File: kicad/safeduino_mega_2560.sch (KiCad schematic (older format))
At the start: 103 parts, among them X1 USB

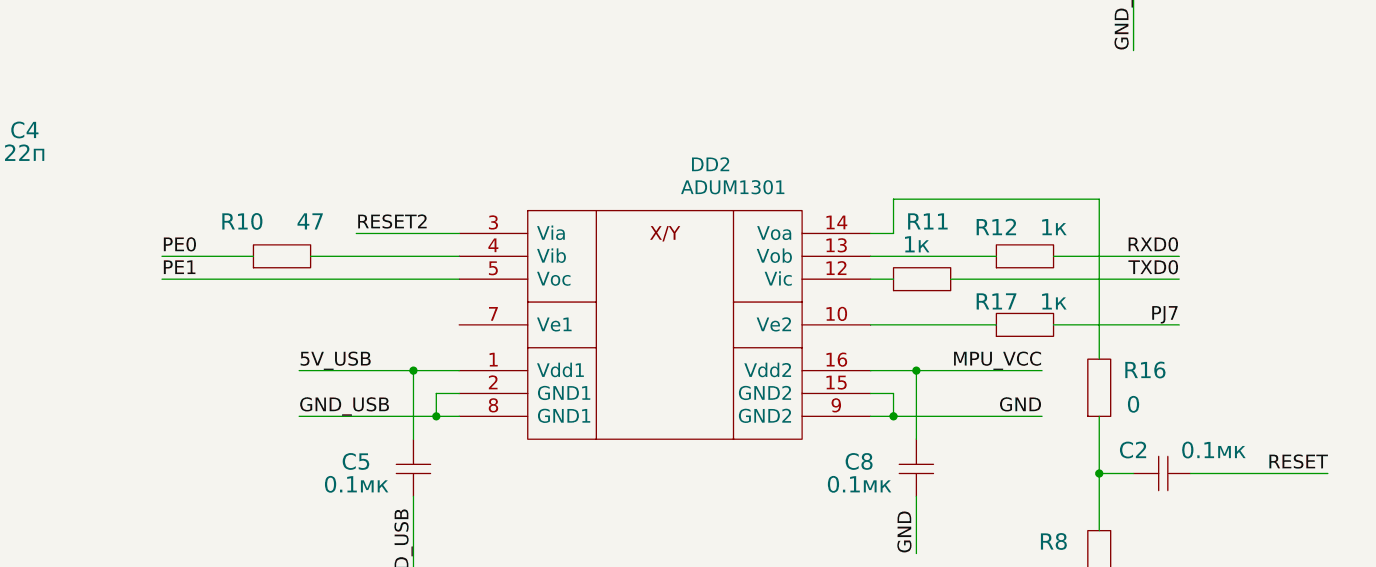
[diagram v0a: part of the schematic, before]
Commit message: Исправил ошибку в подключении ADUM1301.
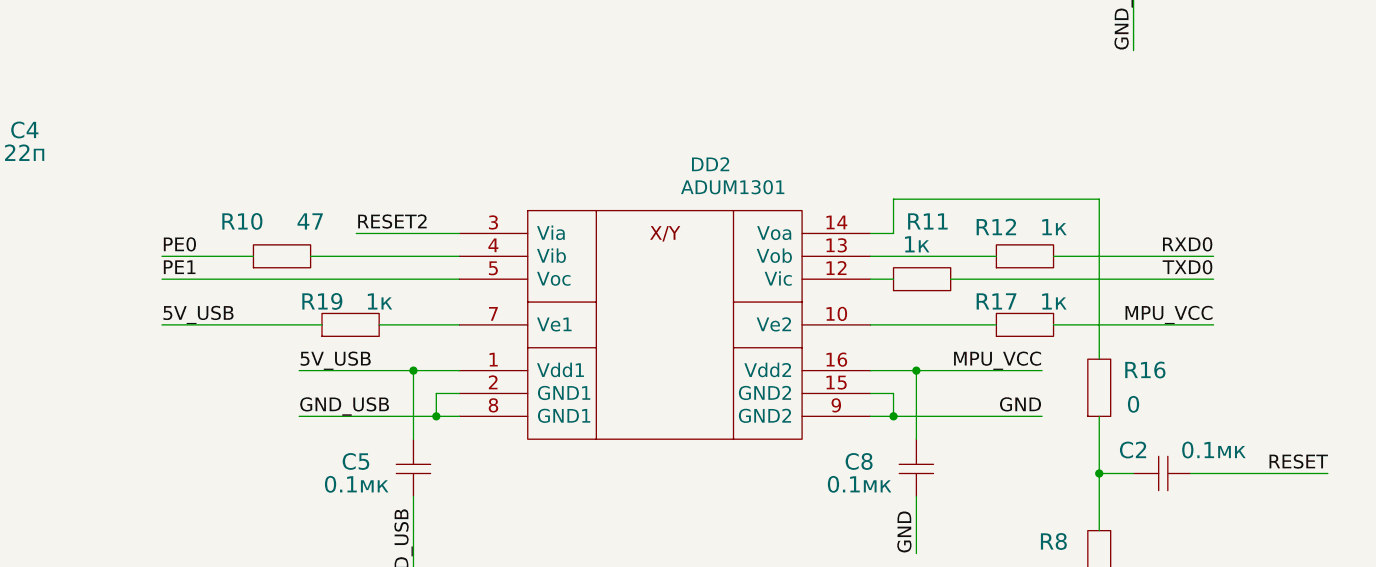
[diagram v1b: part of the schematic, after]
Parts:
- added R19: 1к, symbol RESISTOR
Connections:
- wire segments 420 -> 422
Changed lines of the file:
@@
 Sheet 1 1
 Title "SafeDuino MEGA 2560"
-Date "14 may 2014"
+Date "6 apr 2015"
 Rev ""
 Comp ""
@@
 	17100 4250 15950 4250
 Wire Wire Line
-	9250 10800 9800 10800
+	9250 10800 9950 10800
 Connection ~ 9450 11450
 Wire Wire Line
@@
 	19600 14350 20050 14350
 Wire Wire Line
-	9800 10500 9250 10500
+	9950 10500 9250 10500
 Wire Wire Line
 	8450 10500 9000 10500
@@
 	8450 10600 8550 10600
 Wire Wire Line
-	8800 10600 9800 10600
+	8800 10600 9950 10600
 Wire Wire Line
 	5950 11000 6650 11000
@@
 	1    0    0    1
 $EndComp
-Text Label 9800 10800 2    60   ~ 0
-PJ7
 $Comp
 L RESISTOR R16
@@
 	1    0    0    1
 $EndComp
-Text Label 9800 10600 2    60   ~ 0
+Text Label 9950 10600 2    60   ~ 0
 TXD0
-Text Label 9800 10500 2    60   ~ 0
+Text Label 9950 10500 2    60   ~ 0
 RXD0
 $Comp
@@
 Wire Wire Line
 	4500 7450 4700 7450
+Text Label 9950 10800 2    60   ~ 0
+MPU_VCC
+Wire Wire Line
+	5350 10800 6050 10800
+$Comp
+L RESISTOR R19
+U 1 1 5522B698
+P 6050 10800
+F 0 "R19" H 6050 10700 71  0000 C CNN
+F 1 "1к" H 6300 10700 71  0000 C CNN
+F 2 "" H 6050 10800 60  0001 C CNN
+F 3 "" H 6050 10800 60  0001 C CNN
+	1    6050 10800
+	1    0    0    1
+$EndComp
+Wire Wire Line
+	6300 10800 6650 10800
+Text Label 5350 10800 0    60   ~ 0
+5V_USB
 $EndSCHEMATC

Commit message: Исправил ошибку с сигналом RESER.
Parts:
- added R20: 1к, symbol RESISTOR
- added R21: 1М, symbol RESISTOR
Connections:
- wire segments 422 -> 426
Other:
- note added: "R17 и R19 не устанавливаются на плату\n(используются только для отладки)"
- note added: "R21 необходим для подачи команды RESET на ATMEGA 2560 через\nконденсатор С2"
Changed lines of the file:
@@
 Sheet 1 1
 Title "SafeDuino MEGA 2560"
-Date "6 apr 2015"
+Date "15 apr 2015"
 Rev ""
 Comp ""
@@
 	4250 8750 4700 8750
 Wire Wire Line
-	9450 11950 9450 12450
+	9450 11950 9450 12250
 Wire Wire Line
 	4300 7350 4700 7350
@@
 	13850 10900 13700 10900
 Wire Wire Line
-	13700 10900 13700 10700
+	13700 10700 13700 11000
 Wire Wire Line
 	21400 4900 20950 4900
@@
 	5150 4000 5800 4000
 Wire Wire Line
-	14200 11350 14200 11100
+	14200 11100 14200 11600
 Wire Wire Line
 	20600 11450 20600 11550
@@
 Connection ~ 8550 11200
 Wire Wire Line
-	6200 10400 6650 10400
+	6150 10400 6650 10400
 Wire Wire Line
 	9850 11450 10450 11450
@@
 Text Label 10450 11450 2    60   ~ 0
 RESET
-Text Label 6200 10400 0    60   ~ 0
+Text Label 6150 10400 0    60   ~ 0
 RESET2
 Text Label 8650 11800 1    60   ~ 0
@@
 Text Label 4250 8750 0    60   ~ 0
 RESET2
-Text Label 9450 12450 1    60   ~ 0
-GND_USB
+Text Label 9450 12250 1    60   ~ 0
+GND
 $Comp
 L RESISTOR R8
@@
 	1    0    0    -1
 $EndComp
-Text Label 14200 11350 1    60   ~ 0
+Text Label 14200 11600 1    60   ~ 0
 GND
 $Comp
@@
 Text Label 5350 10800 0    60   ~ 0
 5V_USB
+$Comp
+L RESISTOR R21
+U 1 1 552E6332
+P 13700 11250
+F 0 "R21" V 13900 11450 71  0000 C CNN
+F 1 "1М" V 13750 11450 71  0000 C CNN
+F 2 "" H 13700 11250 60  0001 C CNN
+F 3 "" H 13700 11250 60  0001 C CNN
+	1    13700 11250
+	0    -1   -1   0
+$EndComp
+Connection ~ 13700 10900
+Wire Wire Line
+	13700 11250 13700 11350
+Wire Wire Line
+	13700 11350 14200 11350
+Connection ~ 14200 11350
+$Comp
+L RESISTOR R20
+U 1 1 552E6CCB
+P 6550 10200
+F 0 "R20" V 6750 10400 71  0000 C CNN
+F 1 "1к" V 6600 10400 71  0000 C CNN
+F 2 "" H 6550 10200 60  0001 C CNN
+F 3 "" H 6550 10200 60  0001 C CNN
+	1    6550 10200
+	0    -1   -1   0
+$EndComp
+Wire Wire Line
+	6550 10400 6550 10200
+Connection ~ 6550 10400
+Wire Wire Line
+	6550 9950 6550 9500
+Text Label 6550 9500 3    60   ~ 0
+GND_USB
+Text Notes 6750 12200 0    60   ~ 0
+R17 и R19 не устанавливаются на плату\n(используются только для отладки)
+Text Notes 13250 11800 0    60   ~ 0
+R21 необходим для подачи команды RESET на ATMEGA 2560 через\nконденсатор С2
 $EndSCHEMATC

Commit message: Услучшил разводку платы SafeDuino MEGA 2560.
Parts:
- removed R17, R19: 1к, symbol RESISTOR
- renumbered R20 to R17, R21 to R19
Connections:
- wire segments 426 -> 422
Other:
- note added: "R19 необходим для подачи команды RESET на ATMEGA 2560 через\nконденсатор С2"
- note removed: "R17 и R19 не устанавливаются на плату\n(используются только для отладки)"
- note removed: "R21 необходим для подачи команды RESET на ATMEGA 2560 через\nконденсатор С2"
- moved on the sheet: C2, R19
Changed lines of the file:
@@
 Sheet 1 1
 Title "SafeDuino MEGA 2560"
-Date "15 apr 2015"
+Date "16 apr 2015"
 Rev ""
 Comp ""
@@
 Wire Wire Line
 	17100 4250 15950 4250
-Wire Wire Line
-	9250 10800 9950 10800
 Connection ~ 9450 11450
 Wire Wire Line
 	9450 11200 9450 11700
 Wire Wire Line
-	9600 11450 9450 11450
+	9650 11450 9450 11450
 Wire Wire Line
 	8450 11200 9200 11200
@@
 Wire Wire Line
 	14550 10700 14950 10700
-Wire Wire Line
-	13850 10900 13700 10900
-Wire Wire Line
-	13700 10700 13700 11000
 Wire Wire Line
 	21400 4900 20950 4900
@@
 	6150 10400 6650 10400
 Wire Wire Line
-	9850 11450 10450 11450
+	9900 11450 10650 11450
 Wire Wire Line
 	8450 10400 8550 10400
@@
 Wire Wire Line
 	9450 10250 9450 10950
-Wire Wire Line
-	8450 10800 9000 10800
 Wire Wire Line
 	21400 4300 20950 4300
@@
 PH5
 $Comp
-L RESISTOR R17
-U 1 1 526FBFDF
-P 9000 10800
-F 0 "R17" H 9000 10700 71  0000 C CNN
-F 1 "1к" H 9250 10700 71  0000 C CNN
-F 2 "" H 9000 10800 60  0001 C CNN
-F 3 "" H 9000 10800 60  0001 C CNN
-	1    9000 10800
-	1    0    0    1
-$EndComp
-$Comp
 L RESISTOR R16
 U 1 1 526FBA98
@@
 L CAPITORS C2
 U 1 1 526FBA5B
-P 9850 11450
-F 0 "C2" H 10100 11550 71  0000 C CNN
-F 1 "0.1мк" H 9750 11550 71  0000 C CNN
-F 2 "" H 9850 11450 60  0001 C CNN
-F 3 "" H 9850 11450 60  0001 C CNN
-	1    9850 11450
+P 9900 11450
+F 0 "C2" H 10150 11550 71  0000 C CNN
+F 1 "0.1мк" H 9800 11550 71  0000 C CNN
+F 2 "" H 9900 11450 60  0001 C CNN
+F 3 "" H 9900 11450 60  0001 C CNN
+	1    9900 11450
 	-1   0    0    -1
 $EndComp
-Text Label 10450 11450 2    60   ~ 0
+Text Label 10650 11450 2    60   ~ 0
 RESET
 Text Label 6150 10400 0    60   ~ 0
@@
 Text Label 9950 10800 2    60   ~ 0
 MPU_VCC
-Wire Wire Line
-	5350 10800 6050 10800
 $Comp
 L RESISTOR R19
-U 1 1 5522B698
-P 6050 10800
-F 0 "R19" H 6050 10700 71  0000 C CNN
-F 1 "1к" H 6300 10700 71  0000 C CNN
-F 2 "" H 6050 10800 60  0001 C CNN
-F 3 "" H 6050 10800 60  0001 C CNN
-	1    6050 10800
-	1    0    0    1
-$EndComp
-Wire Wire Line
-	6300 10800 6650 10800
-Text Label 5350 10800 0    60   ~ 0
-5V_USB
-$Comp
-L RESISTOR R21
 U 1 1 552E6332
-P 13700 11250
-F 0 "R21" V 13900 11450 71  0000 C CNN
-F 1 "1М" V 13750 11450 71  0000 C CNN
-F 2 "" H 13700 11250 60  0001 C CNN
-F 3 "" H 13700 11250 60  0001 C CNN
-	1    13700 11250
+P 10150 11950
+F 0 "R19" V 10350 12150 71  0000 C CNN
+F 1 "1М" V 10200 12150 71  0000 C CNN
+F 2 "" H 10150 11950 60  0001 C CNN
+F 3 "" H 10150 11950 60  0001 C CNN
+	1    10150 11950
 	0    -1   -1   0
 $EndComp
-Connection ~ 13700 10900
-Wire Wire Line
-	13700 11250 13700 11350
-Wire Wire Line
-	13700 11350 14200 11350
-Connection ~ 14200 11350
-$Comp
-L RESISTOR R20
+$Comp
+L RESISTOR R17
 U 1 1 552E6CCB
 P 6550 10200
-F 0 "R20" V 6750 10400 71  0000 C CNN
+F 0 "R17" V 6750 10400 71  0000 C CNN
 F 1 "1к" V 6600 10400 71  0000 C CNN
 F 2 "" H 6550 10200 60  0001 C CNN
@@
 Text Label 6550 9500 3    60   ~ 0
 GND_USB
-Text Notes 6750 12200 0    60   ~ 0
-R17 и R19 не устанавливаются на плату\n(используются только для отладки)
-Text Notes 13250 11800 0    60   ~ 0
-R21 необходим для подачи команды RESET на ATMEGA 2560 через\nконденсатор С2
+Text Notes 6200 12550 0    60   ~ 0
+R19 необходим для подачи команды RESET на ATMEGA 2560 через\nконденсатор С2
+Wire Wire Line
+	13700 10700 13700 10900
+Wire Wire Line
+	13700 10900 13850 10900
+Wire Wire Line
+	10150 11700 10150 11450
+Connection ~ 10150 11450
+Wire Wire Line
+	10150 11950 10150 12250
+Text Label 10150 12250 1    60   ~ 0
+GND
 $EndSCHEMATC

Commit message: Исправил неточности в схеме.
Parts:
- C22, C23: value 12.5п -> 12п
- R19: value 1М -> 1M
- XS4: value PBS-6 -> PBS-8
- renumbered XP6 to XP16, XP69 to XP6
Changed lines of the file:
@@
 Sheet 1 1
 Title "SafeDuino MEGA 2560"
-Date "16 apr 2015"
+Date "8 oct 2015"
 Rev ""
 Comp ""
@@
 P 17100 5000
 F 0 "C22" V 17150 5200 71  0000 C CNN
-F 1 "12.5п" V 17250 5250 71  0000 C CNN
+F 1 "12п" V 17250 5200 71  0000 C CNN
 F 2 "" H 17100 5000 60  0001 C CNN
 F 3 "" H 17100 5000 60  0001 C CNN
@@
 P 17600 5000
 F 0 "C23" V 17650 5200 71  0000 C CNN
-F 1 "12.5п" V 17750 5250 71  0000 C CNN
+F 1 "12п" V 17750 5200 71  0000 C CNN
 F 2 "" H 17600 5000 60  0001 C CNN
 F 3 "" H 17600 5000 60  0001 C CNN
@@
 AR Path="/4E2EC900" Ref="XP?"  Part="1"
 AR Path="/4E2ECA5D" Ref="XP?"  Part="1"
-AR Path="/525FE852" Ref="XP6"  Part="1"
-F 0 "XP6" H 16475 12525 50  0000 L BNN
+AR Path="/525FE852" Ref="XP16"  Part="1"
+F 0 "XP16" H 16475 12525 50  0000 L BNN
 F 1 "~" H 16100 12650 50  0000 L BNN
 F 2 "~" H 16500 12700 50  0001 C CNN
@@
 MPU_VCC
 $Comp
-L PIN_M_20 XP69
+L PIN_M_20 XP6
 U 1 1 525BB739
 P 21450 12000
-F 0 "XP69" H 21600 12200 50  0000 L BNN
+F 0 "XP6" H 21600 12200 50  0000 L BNN
 F 1 "IDC-20MS" H 21500 12100 50  0000 L BNN
 F 2 "~" H 21900 12150 50  0001 C CNN
@@
 P 21400 1050
 F 0 "XS4" H 21550 1250 50  0000 L BNN
-F 1 "PBS-6" H 21450 1150 50  0000 L BNN
+F 1 "PBS-8" H 21450 1150 50  0000 L BNN
 F 2 "~" H 21850 1200 50  0001 C CNN
 F 3 "" H 21400 1050 60  0001 C CNN
@@
 P 10150 11950
 F 0 "R19" V 10350 12150 71  0000 C CNN
-F 1 "1М" V 10200 12150 71  0000 C CNN
+F 1 "1M" V 10200 12150 71  0000 C CNN
 F 2 "" H 10150 11950 60  0001 C CNN
 F 3 "" H 10150 11950 60  0001 C CNN

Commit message: Заменил резистор R16 на диод для защиты ADUM от попадания напряжения на входную ногу.
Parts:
- removed R16: 0, symbol RESISTOR
- added VD6: BAS216, symbol DIODE
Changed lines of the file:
@@
 Sheet 1 1
 Title "SafeDuino MEGA 2560"
-Date "8 oct 2015"
+Date "10 mar 2016"
 Rev ""
 Comp ""
@@
 Connection ~ 9450 11450
 Wire Wire Line
-	9450 11200 9450 11700
+	9450 11100 9450 11700
 Wire Wire Line
 	9650 11450 9450 11450
@@
 Connection ~ 11900 10850
 Wire Wire Line
-	11900 11350 11900 10850
+	11900 11100 11900 10850
 Wire Wire Line
 	12050 10400 12150 10400
@@
 	5150 4000 5800 4000
 Wire Wire Line
-	14200 11100 14200 11600
+	14200 11100 14200 11350
 Wire Wire Line
 	20600 11450 20600 11550
@@
 	8550 10250 9450 10250
 Wire Wire Line
-	9450 10250 9450 10950
+	9450 10250 9450 10800
 Wire Wire Line
 	21400 4300 20950 4300
@@
 Text Label 20950 4200 0    60   ~ 0
 PH5
-$Comp
-L RESISTOR R16
-U 1 1 526FBA98
-P 9450 11200
-F 0 "R16" V 9650 11000 71  0000 C CNN
-F 1 "0" V 9500 11050 71  0000 C CNN
-F 2 "" H 9450 11200 60  0001 C CNN
-F 3 "" H 9450 11200 60  0001 C CNN
-	1    9450 11200
-	0    -1   -1   0
-$EndComp
 $Comp
 L CAPITORS C2
@@
 	1    0    0    -1
 $EndComp
-Text Label 11900 11350 1    60   ~ 0
+Text Label 11900 11100 1    60   ~ 0
 GND
 $Comp
@@
 	1    0    0    -1
 $EndComp
-Text Label 14200 11600 1    60   ~ 0
+Text Label 14200 11350 1    60   ~ 0
 GND
 $Comp
@@
 Wire Wire Line
 	4500 7450 4700 7450
-Text Label 9950 10800 2    60   ~ 0
-MPU_VCC
 $Comp
 L RESISTOR R19
@@
 Text Label 10150 12250 1    60   ~ 0
 GND
+$Comp
+L DIODE VD6
+U 1 1 56E17300
+P 9450 10800
+F 0 "VD6" V 9500 11100 71  0000 C CNN
+F 1 "BAS216" V 9600 11100 71  0000 C CNN
+F 2 "" H 9450 10800 60  0001 C CNN
+F 3 "" H 9450 10800 60  0001 C CNN
+	1    9450 10800
+	0    1    1    0
+$EndComp
 $EndSCHEMATC

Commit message: Приступил к разработке новой ревизии платы SafeDuino MEGA 2560 ver. 1.1.
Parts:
- added FU1, FU2: MF-MSMF050, IWsmd_case:SMD1812, symbol LFcomponents:PROTECTOR
- C1, C10, C11, C12, C13, C14, C15, C16, C17, C18, C19, C2, C20, C22, C23, C3, C4, C5, C8, C9: footprint (none) -> IWsmd_case:SMD0805; symbol CAPITORS -> LFcapitors:CAPITORS
- C21, C7: footprint (none) -> IWsmd_case:CASE_B; symbol CAPITORS_ELECTROLYTIC -> LFcapitors:CAPITORS_ELECTROLYTIC
- C6: footprint (none) -> IWsmd_case:CASE_C; symbol CAPITORS_ELECTROLYTIC -> LFcapitors:CAPITORS_ELECTROLYTIC
- DA1: footprint (none) -> IWcomponents:P10LU-0515ZLF; symbol P10LU-0505ELF -> LFcomponents:P10LU-0505ELF
- DA3: footprint (none) -> IWsmd_case:TO_252; symbol LM1117 -> LFcomponents:LM1117
- DD1: footprint (none) -> IWsmd_case:TQFP32_case; symbol ATMEGA16U2-MU -> LFcomponents:ATMEGA16U2-MU
- DD2: value ADUM1301 -> ADUM1301BRWZ; footprint (none) -> IWsmd_case:SOIC16_RW16; symbol ADUM1301 -> LFcomponents:ADUM1301
- DD3: footprint (none) -> IWsmd_case:TQFP100_case; symbol ATMEGA2560-16AU -> LFcomponents:ATMEGA2560-16AU
- R1, R15: footprint (none) -> IWcomponents:Electron_3296W; symbol RESISTOR_TRIMMING -> LFresistor:RESISTOR_TRIMMING
- R10, R11, R12, R13, R14, R17, R18, R19, R2, R3, R4, R5, R6, R7, R8, R9: footprint (none) -> IWsmd_case:SMD0805; symbol RESISTOR -> LFresistor:RESISTOR
- S1: footprint (none) -> IWsmd_case:SWD_BUTTON; symbol BUTTON_SMD_1 -> LFbutton:button_smd_1
- VD1, VD2: footprint (none) -> IWcomponents:SMA; symbol SHOTTKY_DIODE -> LFdiod:SHOTTKY_DIODE
- VD3, VD4: footprint (none) -> IWsmd_case:LED1206; symbol DIODE_LIGHT -> LFdiod:DIODE_LIGHT
- VD5, VD6: footprint (none) -> IWcomponents:SOD110; symbol DIODE -> LFdiod:DIODE
- VT1, VT2: footprint (none) -> IWcomponents:SOT_23; symbol NPN -> LFtransistor:NPN
- X1: footprint ~ -> IWconnectors:CONN_USB-B; symbol USB -> LFconnectors:USB
- XP1, XP2: footprint ~ -> IWconnectors:PIN_ARRAY_3x2; symbol PIN_M_6 -> LFconnectors:connector_6pin_gost
- XP16, XP20, XP21, XP26, XP27, XP28, XP29, XP32, XP36, XP37, XP38, XP39, XP40, XP41, XP42, XP48, XP53, XP54, XP55, XP56, XP57, XP58, XP59, XP60, XP61, XP62, XP65, XP67, XP68, XP7: symbol PIN_M_1 -> LFconnectors:PIN_M_1
- XP3: footprint ~ -> IWconnectors:DG126-5.0-02P-14; symbol PIN_M_2 -> LFconnectors:connector_2pin_gost
- XP4: footprint ~ -> IWconnectors:IDC-16MS; symbol PIN_M_16 -> LFconnectors:connector_16pin_gost
- XP5: footprint ~ -> IWconnectors:PIN_ARRAY_3x1; symbol PIN_M_3 -> LFconnectors:connector_3pin_gost
- XP6: footprint ~ -> IWconnectors:IDC-20MS; symbol PIN_M_20 -> LFconnectors:connector_20pin_gost
- XS1, XS2, XS3, XS4, XS5, XS6, XS7, XS8, XS9: footprint ~ -> IWconnectors:PIN_ARRAY_8x1; symbol PIN_F_8 -> LFconnectors:connector_8pin_gost
- Z1, Z2: footprint (none) -> IWcomponents:HC-49SM; symbol QUARTZ_RESONATOR -> LFcomponents:QUARTZ_RESONATOR
- Z3: footprint (none) -> IWsmd_case:SMD0301M2-2; symbol QUARTZ_RESONATOR -> LFcomponents:QUARTZ_RESONATOR
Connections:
- wire segments 422 -> 484
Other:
- moved on the sheet: C1, R4, R6, VD1, VD3, VD4
